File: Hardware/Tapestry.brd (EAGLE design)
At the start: 96.2 x 67.3 mm, 81 parts, among them U1 ATSAMS70NXXA-AN, U2 AK4618VQ, U3 V_REG_MIC2920, U4 V_REG_MIC2920, Y1 12MHz

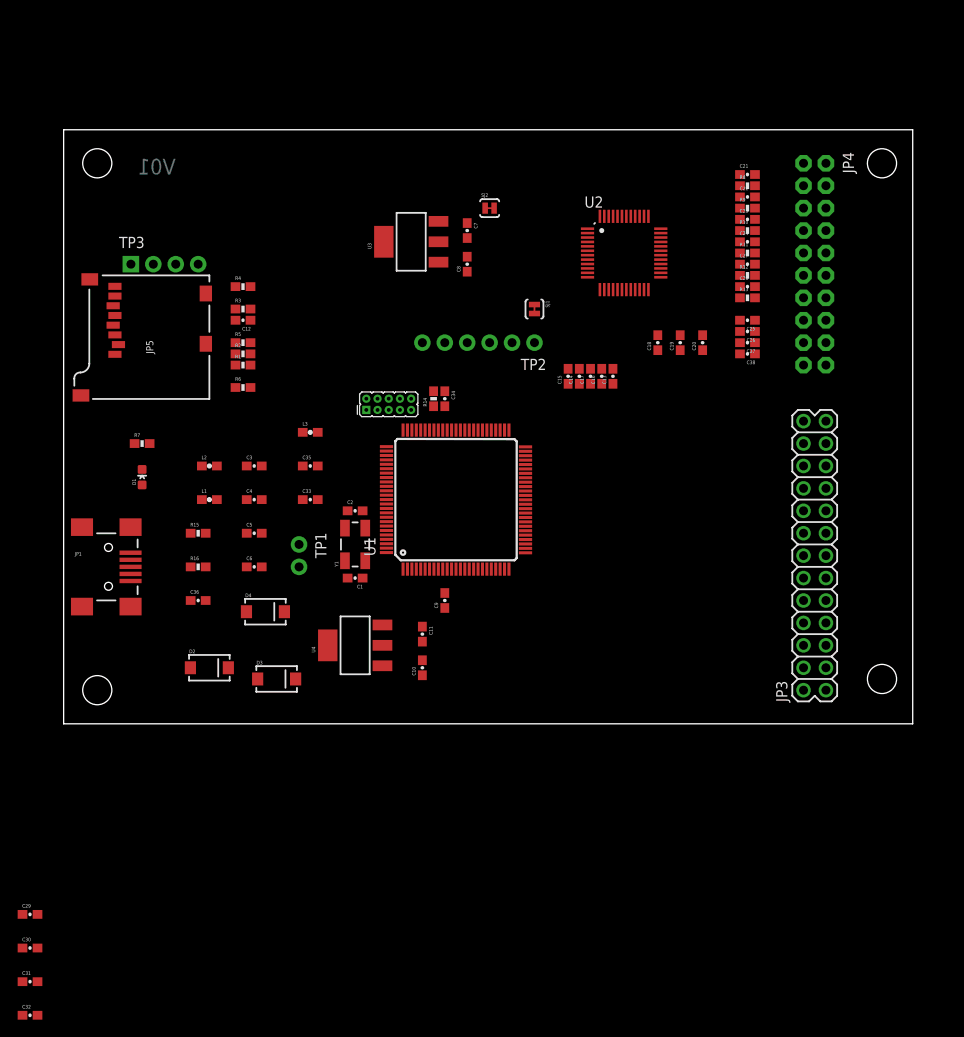
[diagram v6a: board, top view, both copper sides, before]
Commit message: Ongoing progress.
Filled out "layout checklist" in Atmel docs.
Pushed & pulled components to closer to final proximity.
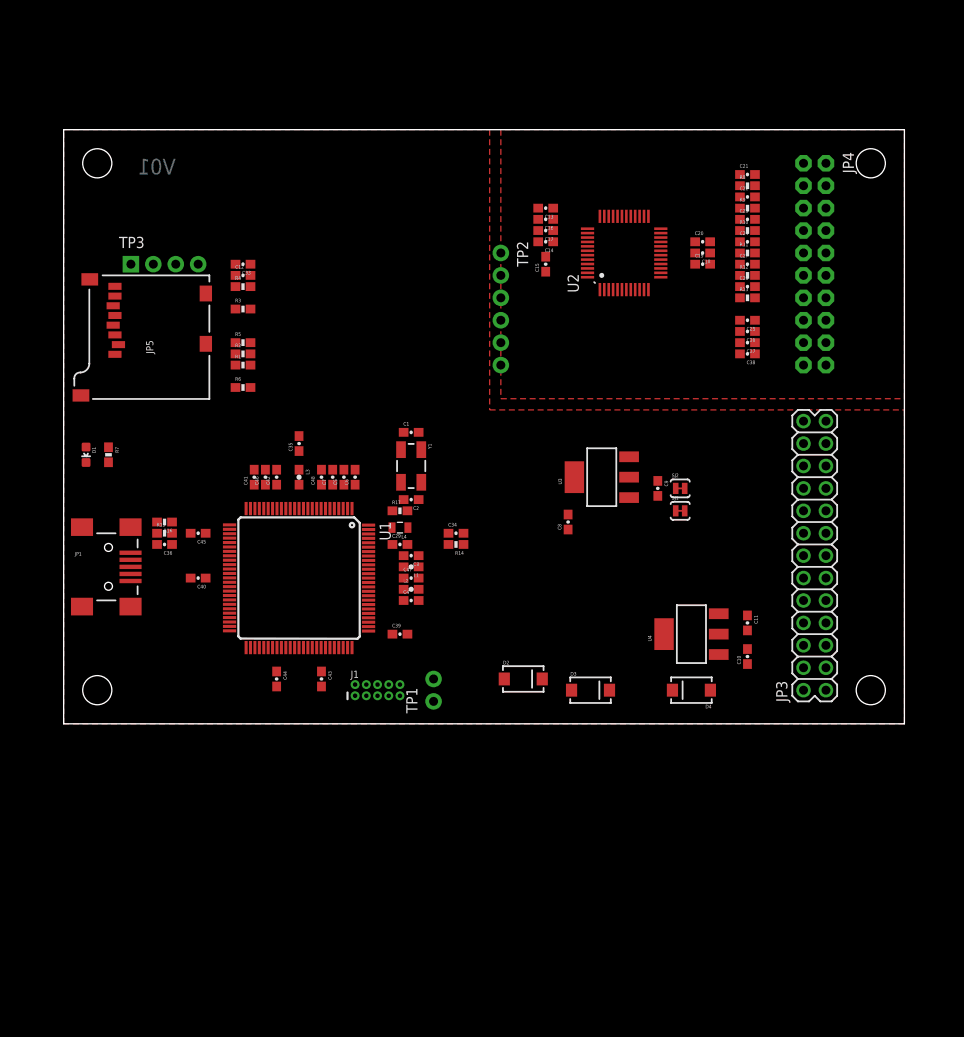
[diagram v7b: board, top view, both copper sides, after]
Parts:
- removed C30, C31, C32: 0.1uF, SparkFun-Capacitors:0603-CAP
- removed JP2: (no value), SparkFun-Connectors:2X5_PTH_SILK_.05
- added C39, C40, C41, C42, C43, C44, C45, C46, C47, C48: 0.1uF, SparkFun-Capacitors:0603-CAP
- added J1: CORTEX_DEBUGPTH, SparkFun-Connectors:2X5-PTH-1.27MM
- added L4: 10uH, SparkFun-Passives:0805
- added R17: 2.2, SparkFun-Resistors:0603-RES
- C29: value 0.1uF -> 4.7uF
- moved C29 59.3 mm to (38.1, 20.3)
- moved D4 49.1 mm to (71.1, 3.81), turned to 180 degrees
- moved SJ2 38.4 mm to (69.8, 26.7)
- moved U4 38.1 mm to (71.1, 10.2)
- moved C10 36.9 mm to (77.5, 7.62)
- moved C11 36.9 mm to (77.5, 11.4)
- moved D2 35.6 mm to (52.1, 5.08)
- moved D3 35.6 mm to (59.7, 3.81)
- moved U3 34.3 mm to (61.0, 27.9)
- moved C7 31.8 mm to (30.5, 27.9), turned to 90 degrees
- moved C8 31.4 mm to (57.1, 22.9)
- moved SJ1 28.2 mm to (69.8, 24.1), turned to 0 degrees
- moved C33 27.7 mm to (20.3, 52.1), turned to 180 degrees
- moved C9 27.3 mm to (67.3, 26.7), turned to 270 degrees
- moved L2 26.8 mm to (39.4, 15.2)
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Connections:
- new net N$24: L4.1, R17.2
- new net VDDOUT: C39.1, C40.1, C41.1, C42.1, C5.1, C6.1, L1.2, L2.2, U1.18, U1.22, U1.39, U1.4, U1.76
- net 3.3V: now also C43.1, C44.1, C45.1, C46.1, C47.1, C48.1, J1.1, R17.1; no longer C29.1, C30.1, C31.1, C32.1, JP2.1, U1.90
- net GND: now also C39.2, C40.2, C41.2, C42.2, C43.2, C44.2, C45.2, C46.2, C47.2, C48.2, J1.3, J1.5, J1.9; no longer C30.2, C31.2, C32.2, JP2.3, JP2.5, JP2.9
- net N$4: now also C29.1, L4.2, U1.90; no longer C5.1, C6.1, L1.2, L2.2, U1.18, U1.22, U1.39, U1.4, U1.76
- net NRESET: now also J1.10; no longer JP2.10
- net SWCLK/TCK: now also J1.4; no longer JP2.4
- net SWDIO/TMS: now also J1.2; no longer JP2.2
- net TDI: now also J1.8; no longer JP2.8
- net TDO: now also J1.6; no longer JP2.6
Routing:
- added copper zone on layer 1, net GND
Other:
- board size 96.2 x 67.3 mm -> 95.2 x 67.3 mm

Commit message: Updates all around
Adjusted LQFP land patterns.
Switched to LM1117 Vregs.
Added library to gitignore.
Ongoing ratsnest work.
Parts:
- added R18, R19: 240, SparkFun-Resistors:0603-RES
- added R20, R21: 390, SparkFun-Resistors:0603-RES
- SJ1, SJ2: value SOLDERJUMPERTRACE -> JUMPER-PAD-2-NC_BY_TRACE; device SparkFun-Retired:SJ_2S-TRACE -> SparkFun-Passives:PAD-JUMPER-2-NC_BY_TRACE_YES_SILK
- U2: value AK4618VQ -> AK4618VQSFE-PACKAGE; device tapestry:LQFP48 -> tapestry:LQFP-48
- U3, U4: value V_REG_MIC2920 -> (none)
- moved JP3 30.6 mm to (83.8, 34.3), turned to 270 degrees
- moved J1 15.2 mm to (20.3, 3.81)
- moved C8 14.8 mm to (69.8, 30.5), turned to 0 degrees
- moved C10 13.7 mm to (69.8, 19.1), turned to 0 degrees
- moved SJ1 12.3 mm to (72.4, 36.2), turned to 90 degrees
- moved D2 11.4 mm to (63.5, 5.08), turned to 90 degrees
- moved U4 9.92 mm to (63.5, 16.5)
- moved SJ2 9.52 mm to (69.8, 36.2), turned to 90 degrees
- moved D3 8.98 mm to (68.6, 5.08), turned to 90 degrees
- moved C11 8.52 mm to (69.8, 15.2)
- moved TP2 6.35 mm to (54.6, 49.5)
- moved C44 3.81 mm to (27.9, 5.08)
- moved C18 3.59 mm to (69.8, 50.8), turned to 270 degrees
- moved D4 2.84 mm to (73.7, 5.08), turned to 90 degrees
- moved C20 2.54 mm to (69.8, 54.6), turned to 270 degrees
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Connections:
- new net N$25: R18.1, R20.2, U3.1
- new net N$29: R19.1, R21.2, U4.1
- net 3.3V: now also JP3.4, R19.2, U4.2, U4.4; no longer U4.3
- net 3.3V_A: now also R18.2, U3.2, U3.4; no longer U3.3
- net AIN1L: now also JP4.13; no longer JP4.1
- net AIN1R: now also JP4.15; no longer JP4.3
- net AIN2L: now also JP4.17; no longer JP4.5
- net AIN2R: now also JP4.19; no longer JP4.7
- net AOUT1L: now also JP4.1; no longer JP4.9
- net AOUT1R: now also JP4.3; no longer JP4.11
- net AOUT2L: now also JP4.5; no longer JP4.13
- net AOUT2R: now also JP4.7; no longer JP4.15
- net AOUT3L: now also JP4.9; no longer JP4.17
- net AOUT3R: now also JP4.11; no longer JP4.19
- net GND: now also R20.1, R21.1; no longer U3.2, U4.2
- net N$9: now also U3.3, U4.3; no longer U3.1, U4.1
